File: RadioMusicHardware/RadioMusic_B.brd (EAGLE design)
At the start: 107 x 19.5 mm, 34 parts, among them IC3 78L05, IC4 TL074, U1 TEENSY_3.1_TW

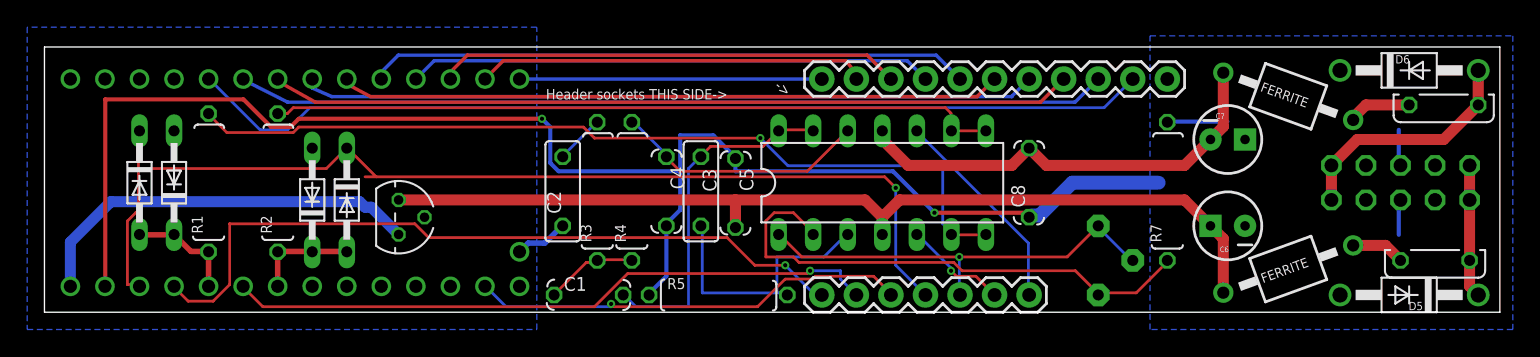
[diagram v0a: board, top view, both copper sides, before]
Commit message: Fix Voltage Regulator + cosmetics rear PCB
Fixes #25
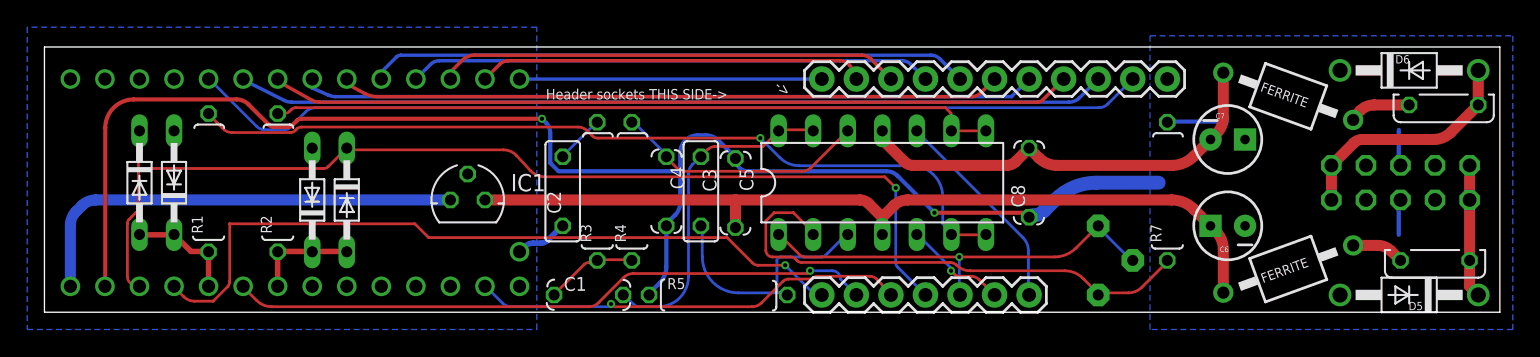
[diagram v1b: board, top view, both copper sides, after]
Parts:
- removed IC3: 78L05, gm-regulators:TO92
- removed U$1: (no value), TW_logos:MTM_1CM
- removed U$3: (no value), TW_logos:CC_1CM_SCREENPRINT
- added IC1: (no value), v-reg:78LXX
- added U$4: (no value), TW_logos:MTM_2CM
- moved U$2 2.54 mm to (39.4, 0.64)
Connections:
- net +12V: now also IC1.IN; no longer IC3.1
- net +5V: now also IC1.OUT; no longer IC3.3
- net DGND: now also IC1.GND; no longer IC3.2
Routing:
- net +12V: track 70.1 -> 63.4 mm
- net +5V: track 29.6 -> 33.4 mm
- net GND: track 122.2 -> 118.8 mm
- net N$6: track 19.8 -> 18.1 mm
- net N$3: track 63.8 -> 62.1 mm
- net +3.3V: track 79.8 -> 78.3 mm
- net N$5: track 25.7 -> 24.3 mm
- net N$7: track 38.9 -> 38.2 mm
- net TIME_POT: track 47.9 -> 47.3 mm
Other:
- board text added: "<-AUDIO OUT"
- board text added: "December 2014 musicthing.co.uk CC-BY-SA"
- board text added: "Inspired by: John Cage Don Buchla Akin Fernandez Stockhausen Nicholas Collins Max Neuhaus UbuWeb Resonance FM John Peel archive.org Thanks to: Paul Stoffregen Steven Thonk The Muff Wigglers"
- board text added: "OUTPUT VOLUME"
- board text added: "Radio Music Back PCB Rev2 Designed in Herne Hill, London by Tom Whitwell"
- board text removed: "<-NB REMEMBER TO INSTALL THIS PIN ON THE TEENSY (AUDIO OUT!)"
- board text removed: "<-Set output volume here"
- board text removed: "Inspired by: John Cage Don Buchla Stockhausen Nicholas Collins Max Neuhaus, Akin Fernandez UbuWeb Resonance FM Thanks to: Paul Stoffregen, Steven Thonk The Muff Wigglers"
- board text removed: "Radio Music Back PCB Rev 1 Designed in Herne Hill, London by Tom Whitwell October 2014 CC-BY-SA musicthing.co.uk"
